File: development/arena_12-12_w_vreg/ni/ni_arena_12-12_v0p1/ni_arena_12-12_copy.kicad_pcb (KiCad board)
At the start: 4 copper layers, 228.6 x 228.6 mm, 126 parts, among them J1 Barrel_Jack, J2 NI_TE_68pos, P1 CONN15, P10 CONN15, P11 CONN15, P12 CONN15, P2 CONN15, P3 CONN15, P4 CONN15, P5 CONN15, P6 CONN15, P7 CONN15, P8 CONN15, P9 CONN15, Q2 MOSFET_NCHAN, SW1 SW_SPDT, U1 TXB0108PW, U10 TPS564201DDC, U11 TPS564201DDC, U12 TPS564201DDC, U13 TPS564201DDC, U14 TPS564201DDC, U15 TPS564201DDC, U16 TPS564201DDC, U17 TPS564201DDC, U18 AP2112K-3.3, U2 TXB0108PW, U3 TXB0108PW, U4 TXB0108PW, U5 TXB0108PW, U6 TPS564201DDC, U7 TPS564201DDC, U8 TPS564201DDC, U9 TPS564201DDC

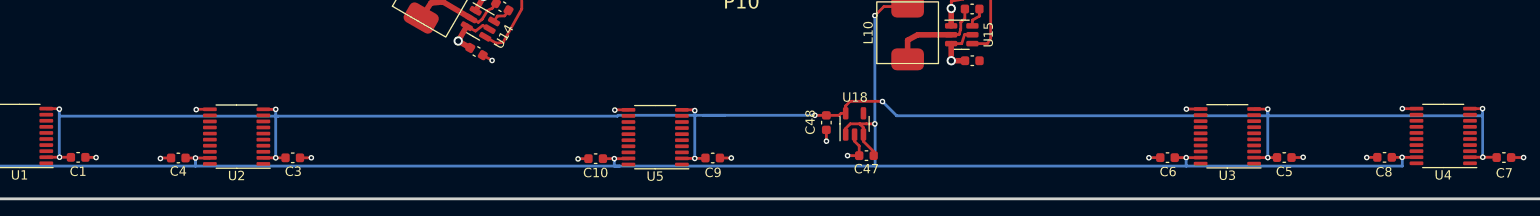
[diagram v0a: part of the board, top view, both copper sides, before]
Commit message: Modified ni 12-12 arena with vreg to be 6-layers.
Stack up is sig, gnd, vcc, 3v3, gnd,  sig.
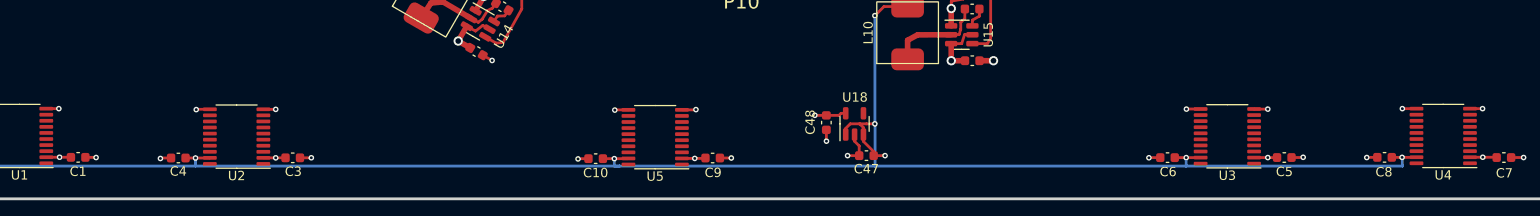
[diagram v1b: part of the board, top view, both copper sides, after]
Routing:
- net +3.3V: track 202.9 -> 23.4 mm, vias 12 -> 11
- net GND: track 136.0 -> 137.5 mm, vias 41 -> 42
- net /Level Shifters/POW.5V_HDR_10: track 213.9 -> 215.1 mm, vias 7 -> 8
- added copper zone on In3.Cu, net +3.3V
- added copper zone on In4.Cu, net GND
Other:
- copper layers 4 -> 6
